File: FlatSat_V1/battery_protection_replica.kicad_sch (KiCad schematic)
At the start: 50 parts, among them J500 BENCH PSU B+/MID/B-, J510 USB-C CHARGER IN (power only), Q500 IRF7458, Q501 IRF7458, Q510 DMP4047LFDE-7, U500 R5460N208AA-TR-FE, U510 DZDH0401DW-7, U511 BQ25886RGE

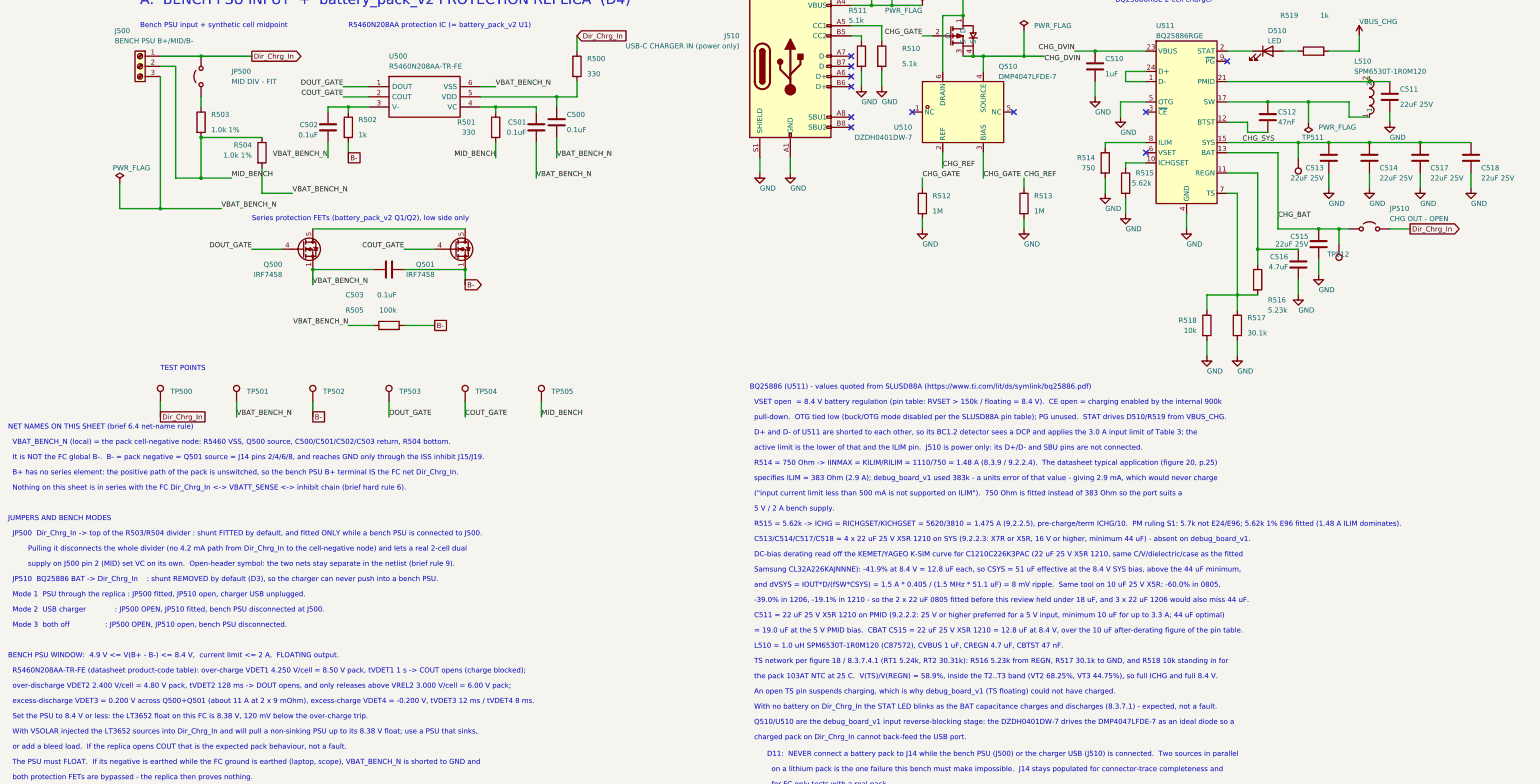
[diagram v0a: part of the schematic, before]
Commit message: FlatSat V1: apply pre-order review fix-this-rev items 1,2,3,4,6,7
1 Mode 2 feeds the FC from BQ25886 SYS (JP510.1 -> CHG_SYS), 78 -> 24 mOhm.
2 Dir_Chrg_In attaches at J14.1 (In1 1.5 mm L11 stub); J16.8 stub and
  its 140 mm / 5-via run removed. J500.1->J14.1 307 -> 35 mOhm.
3 Replica sense-loop copper 68 -> 8 mOhm; excess-discharge trip
  ~2.3 A -> ~7.7 A. Kelvin VSS tap at Q500 source.
4 BQ25886: C513 at the SYS pins, 9 EP thermal PTH pads (U18 convention),
  GND vias at every charger cap, SW 0.8 mm, PMID 1.0 mm on F.Cu.
6 bench_power_width DRC rule (warning, outside FC_COPY), 7 power nodes
  labelled into BenchPower, BenchPower5V for CHG_DVIN.
7 VSOLAR bench hard maximum 18 V (heritage C40 is 10 V), 18V MAX silk.

Gates: heritage refill 0, attachment 0/7/37, DRC 14/1/11, ERC 12,
via-in-pad 7. Edit scripts kept under review_fixes_scripts/.

Co-Authored-By: Claude Opus 5.5 (1M context) <noreply@anthropic.com>
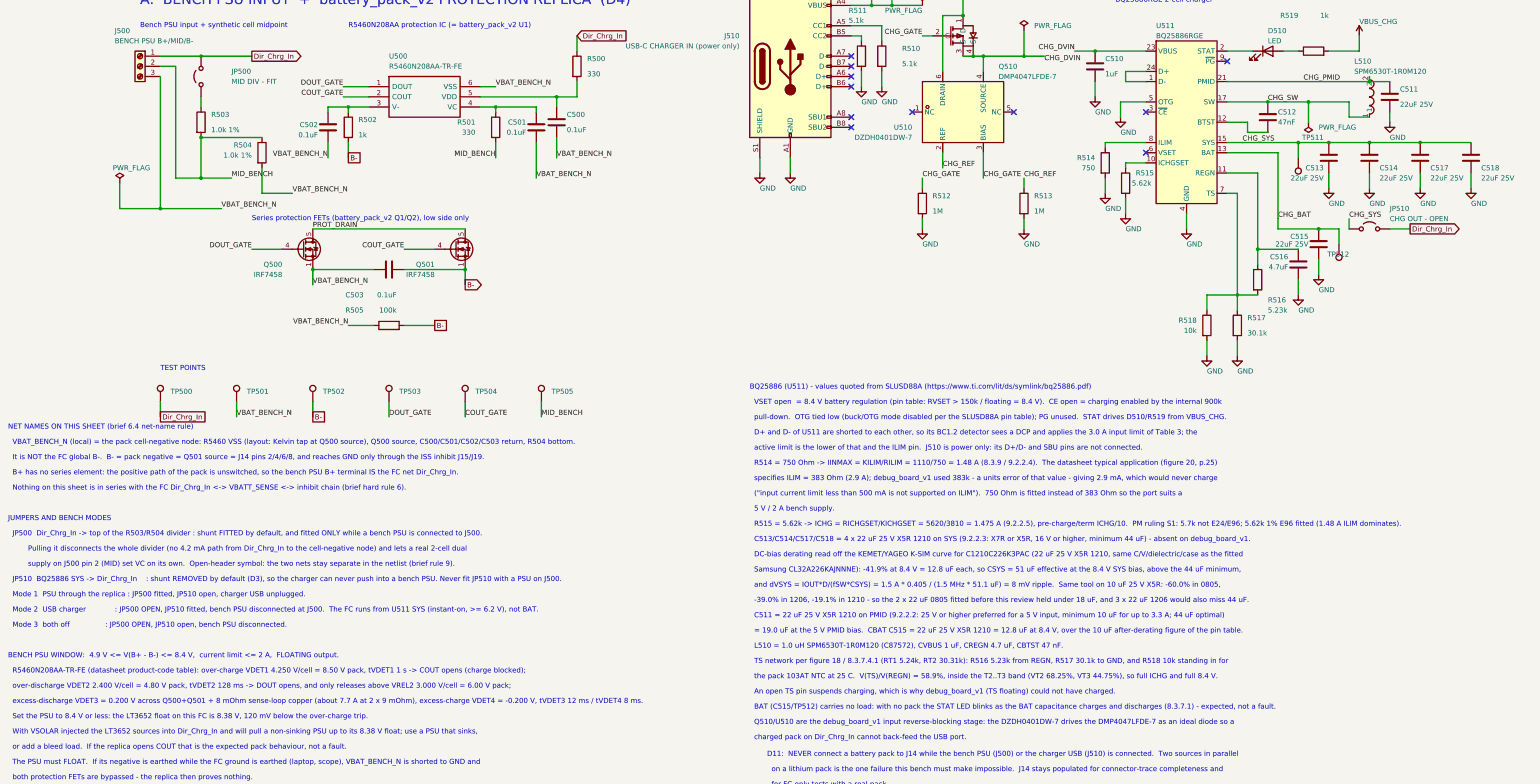
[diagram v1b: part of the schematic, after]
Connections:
- net CHG_BAT: no longer JP510.1 (A)
- net CHG_SYS: now also JP510.1 (A)
- net CHG_PMID: now reaches C511.1, L510.2, U511.21 (PMID), U511.22 (PMID)
- net CHG_SW: now reaches C512.1, L510.1, U511.17 (SW), U511.18 (SW)
- net PROT_DRAIN: now reaches Q500.5 (D), Q500.6 (D), Q500.7 (D), Q500.8 (D), Q501.5 (D), Q501.6 (D), Q501.7 (D), Q501.8 (D)
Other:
- note added: "BAT (C515/TP512) carries no load: with no pack the STAT LED blinks as the BAT capacitance charges and discharges (8.3.7.1) - expected, not a fault."
- note added: "JP510 BQ25886 SYS -> Dir_Chrg_In : shunt REMOVED by default (D3), so the charger can never push into a bench PSU. Never fit JP510 with a PSU on J500."
- note added: "Mode 2 USB charger : JP500 OPEN, JP510 fitted, bench PSU disconnected at J500. The FC runs from U511 SYS (instant-on, >= 6.2 V), not BAT."
- note added: "VBAT_BENCH_N (local) = the pack cell-negative node: R5460 VSS (layout: Kelvin tap at Q500 source), Q500 source, C500/C501/C502/C503 return, R504 bottom."
- note added: "excess-discharge VDET3 = 0.200 V across Q500+Q501 + 8 mOhm sense-loop copper (about 7.7 A at 2 x 9 mOhm), excess-charge VDET4 = -0.200 V, tVDET3 12 ms / tVDET4 8 ms."
- note removed: "JP510 BQ25886 BAT -> Dir_Chrg_In : shunt REMOVED by default (D3), so the charger can never push into a bench PSU."
- note removed: "Mode 2 USB charger : JP500 OPEN, JP510 fitted, bench PSU disconnected at J500."
- note removed: "VBAT_BENCH_N (local) = the pack cell-negative node: R5460 VSS, Q500 source, C500/C501/C502/C503 return, R504 bottom."
- note removed: "With no battery on Dir_Chrg_In the STAT LED blinks as the BAT capacitance charges and discharges (8.3.7.1) - expected, not a fault."
- note removed: "excess-discharge VDET3 = 0.200 V across Q500+Q501 (about 11 A at 2 x 9 mOhm), excess-charge VDET4 = -0.200 V, tVDET3 12 ms / tVDET4 8 ms."
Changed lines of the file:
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@@
 		)
 	)
+	(label "PROT_DRAIN"
+		(at 91.44 101.6 0)
+		(effects
+			(font
+				(size 1.27 1.27)
+			)
+			(justify left bottom)
+		)
+	)
+	(label "CHG_PMID"
+		(at 339.09 64.77 0)
+		(effects
+			(font
+				(size 1.27 1.27)
+			)
+			(justify left bottom)
+		)
+	)
+	(label "CHG_SW"
+		(at 330.2 69.85 0)
+		(effects
+			(font
+				(size 1.27 1.27)
+			)
+			(justify left bottom)
+		)
+	)
+	(wire
+		(pts
+			(xy 350.52 101.6) (xy 350.52 99.06)
+		)
+		(stroke
+			(width 0)
+			(type default)
+		)
+	)
+	(label "CHG_SYS"
+		(at 350.52 99.06 0)
+		(effects
+			(font
+				(size 1.27 1.27)
+			)
+			(justify left bottom)
+		)
+	)
 	(wire
 		(pts
@@
 	(wire
 		(pts
-			(xy 342.9 101.6) (xy 350.52 101.6)
+			(xy 342.9 101.6) (xy 347.98 101.6)
 		)
 		(stroke
@@
 		(color 0 0 0 0)
 	)
-	(junction
-		(at 347.98 101.6)
-		(diameter 0)
-		(color 0 0 0 0)
-	)
 	(symbol
 		(lib_id "Device:C")
@@
 			)
 		)
-		(property "Description" "Test point, BQ25886 BAT (charger output, before JP510)"
+		(property "Description" "Test point, BQ25886 BAT (CBAT C515 only; JP510 is fed from SYS)"
 			(at 347.98 105.41 0)
 			(hide yes)
@@
 			)
 		)
-		(property "Description" "2-pin header, shunt REMOVED by default (D3): charger BAT -> Dir_Chrg_In"
+		(property "Description" "2-pin header, shunt REMOVED by default (D3): charger SYS -> Dir_Chrg_In"
 			(at 355.6 101.6 0)
 			(hide yes)
@@
 		)
 	)
-	(text "  VBAT_BENCH_N (local) = the pack cell-negative node: R5460 VSS, Q500 source, C500/C501/C502/C503 return, R504 bottom."
+	(text "  VBAT_BENCH_N (local) = the pack cell-negative node: R5460 VSS (layout: Kelvin tap at Q500 source), Q500 source, C500/C501/C502/C503 return, R504 bottom."
 		(exclude_from_sim no)
 		(at 15.24 155 0)
@@
 		)
 	)
-	(text "  JP510  BQ25886 BAT -> Dir_Chrg_In    : shunt REMOVED by default (D3), so the charger can never push into a bench PSU."
+	(text "  JP510  BQ25886 SYS -> Dir_Chrg_In    : shunt REMOVED by default (D3), so the charger can never push into a bench PSU. Never fit JP510 with a PSU on J500."
 		(exclude_from_sim no)
 		(at 15.24 189.29 0)
@@
 		)
 	)
-	(text "  Mode 2  USB charger             : JP500 OPEN, JP510 fitted, bench PSU disconnected at J500."
+	(text "  Mode 2  USB charger             : JP500 OPEN, JP510 fitted, bench PSU disconnected at J500.  The FC runs from U511 SYS (instant-on, >= 6.2 V), not BAT."
 		(exclude_from_sim no)
 		(at 15.24 196.91 0)
@@
 		)
 	)
-	(text "  excess-discharge VDET3 = 0.200 V across Q500+Q501 (about 11 A at 2 x 9 mOhm), excess-charge VDET4 = -0.200 V, tVDET3 12 ms / tVDET4 8 ms."
+	(text "  excess-discharge VDET3 = 0.200 V across Q500+Q501 + 8 mOhm sense-loop copper (about 7.7 A at 2 x 9 mOhm), excess-charge VDET4 = -0.200 V, tVDET3 12 ms / tVDET4 8 ms."
 		(exclude_from_sim no)
 		(at 15.24 219.77 0)
@@
 		)
 	)
-	(text "  With no battery on Dir_Chrg_In the STAT LED blinks as the BAT capacitance charges and discharges (8.3.7.1) - expected, not a fault."
+	(text "  BAT (C515/TP512) carries no load: with no pack the STAT LED blinks as the BAT capacitance charges and discharges (8.3.7.1) - expected, not a fault."
 		(exclude_from_sim no)
 		(at 200.66 221.2 0)

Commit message: FlatSat V1: apply review pass 2 fix-this-rev items 1-3
1 J510 moved to (262.0,168.93): shell face 0.46 mm proud of the edge per
  the HRO drawing (was 2.41 mm recessed); escapes stretched, no new copper.
2 J500 over-voltage block on the battery sheet (OVP <= 9 V, trip check,
  never the VSOLAR supply) and 8.4V MAX silk.
3 Gate-drive probing note (TP501-TP504 reference floating nets) on the
  sheet and in the review ATP text. Item 6 Mode 2 ISS-bypass note added.

Gates: heritage refill 0, attachment 0/7/37, DRC 14/1/11 (item set
unchanged), via-in-pad 0/0, track_width 95, ERC 12.

Co-Authored-By: Claude Opus 5.5 (1M context) <noreply@anthropic.com>
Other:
- note added: "BENCH PSU WINDOW: 4.9 V <= V(B+ - B-) <= 8.4 V, current limit <= 2 A, FLOATING output. PSU OVP <= 9 V: see J500 OVER-VOLTAGE, right."
- note added: "GATE-DRIVE PROBING (TP501-TP504):"
- note added: "J500 OVER-VOLTAGE (no OV element on J500 this rev; legend 8.4V MAX on the board):"
- note added: "JP606/RBF; run ISS-inhibit, deployment-switch and protection-trip tests in"
- note added: "MODE 2 returns through board GND: the ISS inhibit (J15/J19/JP607) and the R5460"
- note added: "Measure gate drive with a floating DMM, a differential probe or an isolated"
- note added: "Mode 1 only."
- note added: "Mode 2 USB charger : JP500 OPEN, JP510 fitted, bench PSU disconnected at J500. The FC runs from U511 SYS (instant-on, >= 6.2 V), not BAT. See MODE 2 note, right."
- note added: "PSU OVP <= 9 V; verify the trip with J500 disconnected before each session;"
- note added: "TP501/TP503 are referenced to VBAT_BENCH_N and TP502/TP504 to B-, not GND."
- note added: "never use the 12-18 V VSOLAR supply on J500 (heritage C42/C1/C3 are 10 V"
- note added: "rated, U500 VDD abs max 12 V)."
- note added: "read gates relative to TP501/TP502 by subtraction. Never earth TP501 or J500.3"
- note added: "replica are NOT in circuit; JP607 is needed in Mode 1 only; safe the bus with"
- note added: "scope; or clip the scope ground to board GND (JP607.2) with JP607 closed and"
- note added: "while J701 or FC USB is on an earthed host."
- note removed: "BENCH PSU WINDOW: 4.9 V <= V(B+ - B-) <= 8.4 V, current limit <= 2 A, FLOATING output."
- note removed: "Mode 2 USB charger : JP500 OPEN, JP510 fitted, bench PSU disconnected at J500. The FC runs from U511 SYS (instant-on, >= 6.2 V), not BAT."
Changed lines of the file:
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@@
 		)
 	)
+	(text "J500 OVER-VOLTAGE (no OV element on J500 this rev; legend 8.4V MAX on the board):"
+		(exclude_from_sim no)
+		(at 205 248.25 0)
+		(effects
+			(font
+				(size 1.27 1.27)
+			)
+			(justify left bottom)
+		)
+	)
+	(text "  PSU OVP <= 9 V; verify the trip with J500 disconnected before each session;"
+		(exclude_from_sim no)
+		(at 205 252.06 0)
+		(effects
+			(font
+				(size 1.27 1.27)
+			)
+			(justify left bottom)
+		)
+	)
+	(text "  never use the 12-18 V VSOLAR supply on J500 (heritage C42/C1/C3 are 10 V"
+		(exclude_from_sim no)
+		(at 205 255.87 0)
+		(effects
+			(font
+				(size 1.27 1.27)
+			)
+			(justify left bottom)
+		)
+	)
+	(text "  rated, U500 VDD abs max 12 V)."
+		(exclude_from_sim no)
+		(at 205 259.68 0)
+		(effects
+			(font
+				(size 1.27 1.27)
+			)
+			(justify left bottom)
+		)
+	)
+	(text "MODE 2 returns through board GND: the ISS inhibit (J15/J19/JP607) and the R5460"
+		(exclude_from_sim no)
+		(at 205 267.3 0)
+		(effects
+			(font
+				(size 1.27 1.27)
+			)
+			(justify left bottom)
+		)
+	)
+	(text "  replica are NOT in circuit; JP607 is needed in Mode 1 only; safe the bus with"
+		(exclude_from_sim no)
+		(at 205 271.11 0)
+		(effects
+			(font
+				(size 1.27 1.27)
+			)
+			(justify left bottom)
+		)
+	)
+	(text "  JP606/RBF; run ISS-inhibit, deployment-switch and protection-trip tests in"
+		(exclude_from_sim no)
+		(at 205 274.92 0)
+		(effects
+			(font
+				(size 1.27 1.27)
+			)
+			(justify left bottom)
+		)
+	)
+	(text "  Mode 1 only."
+		(exclude_from_sim no)
+		(at 205 278.73 0)
+		(effects
+			(font
+				(size 1.27 1.27)
+			)
+			(justify left bottom)
+		)
+	)
+	(text "GATE-DRIVE PROBING (TP501-TP504):"
+		(exclude_from_sim no)
+		(at 142.24 102.87 0)
+		(effects
+			(font
+				(size 1.27 1.27)
+			)
+			(justify left bottom)
+		)
+	)
+	(text "  TP501/TP503 are referenced to VBAT_BENCH_N and TP502/TP504 to B-, not GND."
+		(exclude_from_sim no)
+		(at 142.24 106.68 0)
+		(effects
+			(font
+				(size 1.27 1.27)
+			)
+			(justify left bottom)
+		)
+	)
+	(text "  Measure gate drive with a floating DMM, a differential probe or an isolated"
+		(exclude_from_sim no)
+		(at 142.24 110.49 0)
+		(effects
+			(font
+				(size 1.27 1.27)
+			)
+			(justify left bottom)
+		)
+	)
+	(text "  scope; or clip the scope ground to board GND (JP607.2) with JP607 closed and"
+		(exclude_from_sim no)
+		(at 142.24 114.3 0)
+		(effects
+			(font
+				(size 1.27 1.27)
+			)
+			(justify left bottom)
+		)
+	)
+	(text "  read gates relative to TP501/TP502 by subtraction.  Never earth TP501 or J500.3"
+		(exclude_from_sim no)
+		(at 142.24 118.11 0)
+		(effects
+			(font
+				(size 1.27 1.27)
+			)
+			(justify left bottom)
+		)
+	)
+	(text "  while J701 or FC USB is on an earthed host."
+		(exclude_from_sim no)
+		(at 142.24 121.92 0)
+		(effects
+			(font
+				(size 1.27 1.27)
+			)
+			(justify left bottom)
+		)
+	)
 	(wire
 		(pts
@@
 		)
 	)
-	(text "  Mode 2  USB charger             : JP500 OPEN, JP510 fitted, bench PSU disconnected at J500.  The FC runs from U511 SYS (instant-on, >= 6.2 V), not BAT."
+	(text "  Mode 2  USB charger             : JP500 OPEN, JP510 fitted, bench PSU disconnected at J500.  The FC runs from U511 SYS (instant-on, >= 6.2 V), not BAT.  See MODE 2 note, right."
 		(exclude_from_sim no)
 		(at 15.24 196.91 0)
@@
 		)
 	)
-	(text "BENCH PSU WINDOW:  4.9 V <= V(B+ - B-) <= 8.4 V,  current limit <= 2 A,  FLOATING output."
+	(text "BENCH PSU WINDOW:  4.9 V <= V(B+ - B-) <= 8.4 V,  current limit <= 2 A,  FLOATING output.  PSU OVP <= 9 V: see J500 OVER-VOLTAGE, right."
 		(exclude_from_sim no)
 		(at 15.24 208.34 0)

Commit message: FlatSat V1: fix 8 wrong-part LCSC fields; header collapse; sync project.db
35 Phase-1/2 footprints carried a stale board-only LCSC field cloned
from heritage footprints; the JLC plugin reads it before LCSC Part, so
8 would have been ordered wrong: C221/C222 (15 pF) and C301 (10 nF) and
C304 (1 uF) as C1525 100 nF; D201/D202/D510/LED600 as C12624. Removed
the stale field from all 35 (fields only, no geometry).

PLM-08: the 13 identical 1x02 headers now all use C492401. U1 LCSC field
-> C181596 (TSSOP, matches project.db and Rev2).

project.db synced with JLCPCB Tools release 2026.04.03's own Store code
(owner request 2026-10-22): 258 -> 481 rows, 223 added, 0 changed.

Gates unchanged: heritage refill 0, attachment 0/7/37, DRC 14/1/11,
via-in-pad 0/0, ERC 12.

Co-Authored-By: Claude Opus 5.5 (1M context) <noreply@anthropic.com>
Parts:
- JP500, JP510: LCSC Part C358684 -> C492401
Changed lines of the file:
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@@
 			)
 		)
-		(property "Datasheet" "https://www.lcsc.com/product-detail/C358684.html"
+		(property "Datasheet" "https://www.lcsc.com/datasheet/lcsc_datasheet_2409302300_XFCN-PZ254V-11-02P_C492401.pdf"
 			(at 63.5 63.5 0)
 			(hide yes)
@@
 			)
 		)
-		(property "LCSC Part" "C358684"
+		(property "LCSC Part" "C492401"
 			(at 63.5 63.5 0)
 			(hide yes)
@@
 			)
 		)
-		(property "Datasheet" "https://www.lcsc.com/product-detail/C358684.html"
+		(property "Datasheet" "https://www.lcsc.com/datasheet/lcsc_datasheet_2409302300_XFCN-PZ254V-11-02P_C492401.pdf"
 			(at 355.6 101.6 0)
 			(hide yes)
@@
 			)
 		)
-		(property "LCSC Part" "C358684"
+		(property "LCSC Part" "C492401"
 			(at 355.6 101.6 0)
 			(hide yes)
